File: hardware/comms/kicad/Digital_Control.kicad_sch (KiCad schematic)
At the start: 9 parts, among them J6 Conn_01x20, J7 Conn_01x20, J8 Conn_01x20

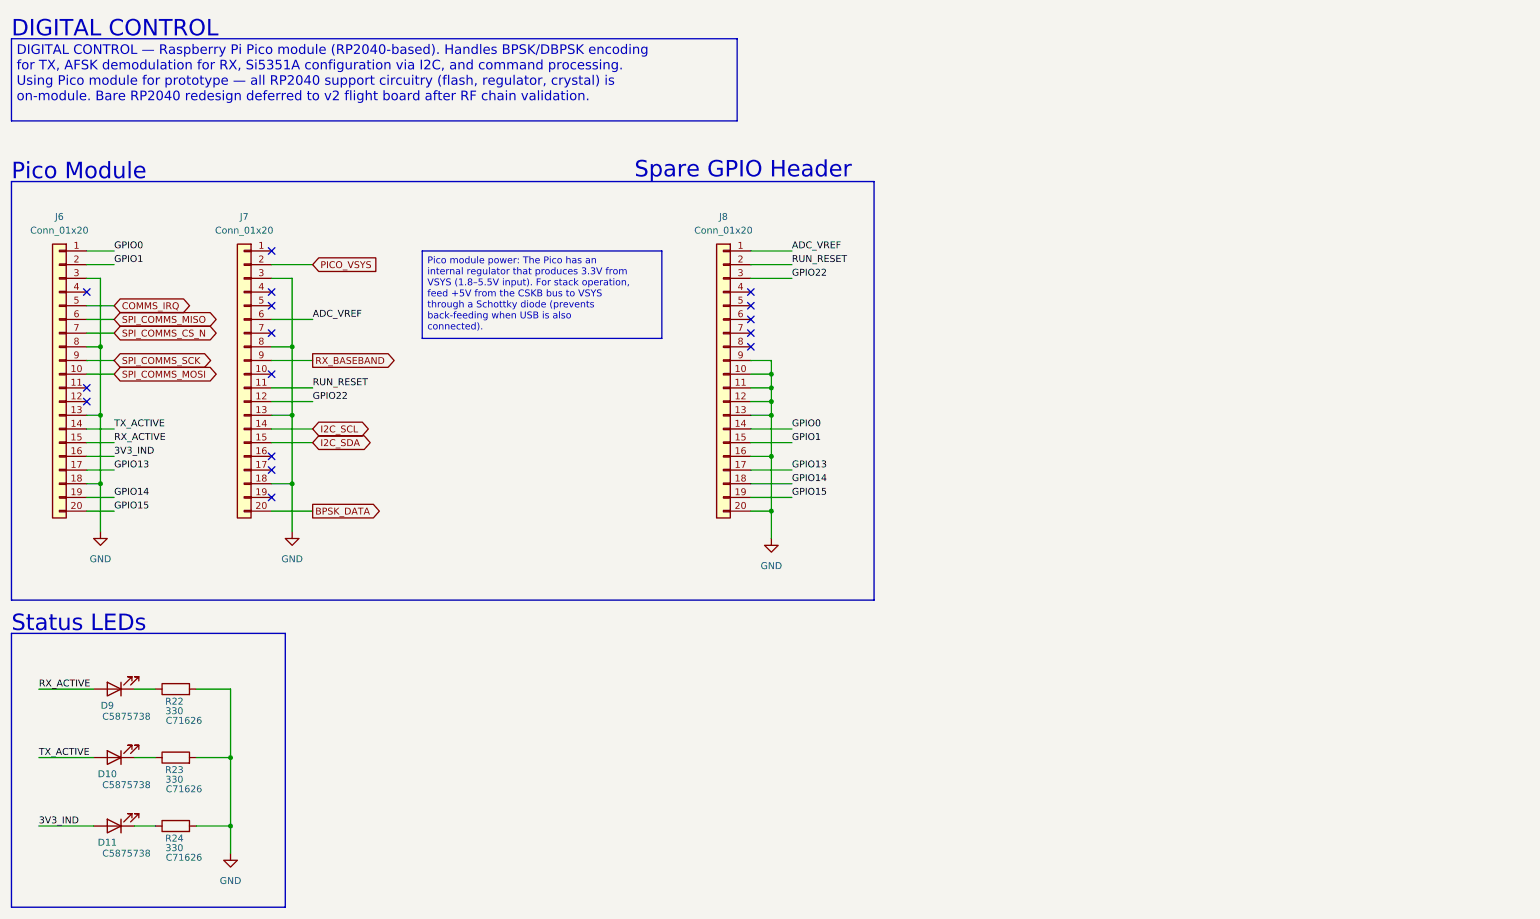
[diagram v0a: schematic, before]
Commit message: comms: checkpoint current KiCad design before ground station work
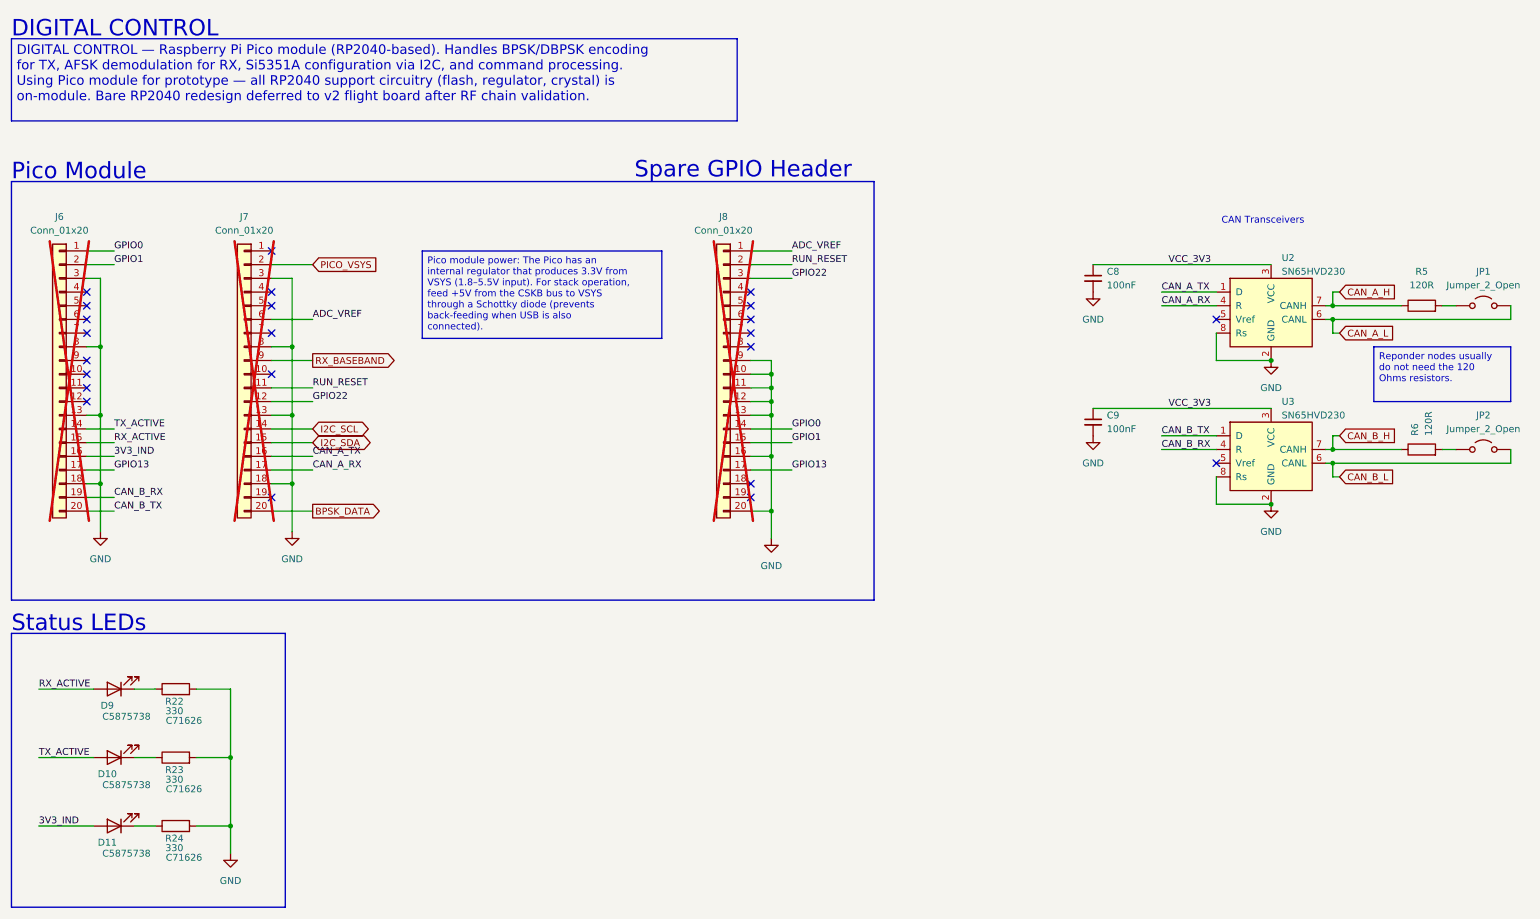
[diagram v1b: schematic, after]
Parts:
- added C8, C9: 100nF, Capacitor_SMD:C_0805_2012Metric, symbol Device:C_Small
- added JP1, JP2: Jumper_2_Open, Connector_PinHeader_2.54mm:PinHeader_1x02_P2.54mm_Vertical, symbol Jumper:Jumper_2_Open
- added R5, R6: 120R, Resistor_SMD:R_0805_2012Metric, symbol Device:R
- added U2, U3: SN65HVD230, Package_SO:SOIC-8_3.9x4.9mm_P1.27mm, symbol Interface_CAN_LIN:SN65HVD230
- J6, J7: footprint (none) -> Connector_PinHeader_2.54mm:PinHeader_1x20_P2.54mm_Vertical; AssemblyNote (none) -> DNP - optional 1x20 2.54mm through-hole header; do not popu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; LCSC Part # ESQ-120-14-G-S -> (none); now not fitted
- J8: footprint (none) -> Connector_PinHeader_2.54mm:PinHeader_1x20_P2.54mm_Vertical; Assembly Note (none) -> DNP - optional 1x20 2.54mm through-hole expansion header; p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; AssemblyNote (none) -> DNP - optional 1x20 2.54mm through-hole header; do not popu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; LCSC Part # ESQ-120-14-G-S -> (none); now not fitted
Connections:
- net GND: now also C8.2, C9.2, U2.2 (GND), U2.8 (Rs), U3.2 (GND), U3.8 (Rs)
- net CAN_A_TX: now reaches J7.16 (Pin_16)
- net CAN_A_TX: now also U2.1 (D)
- net CAN_A_RX: now reaches J7.17 (Pin_17)
- net CAN_A_RX: now also U2.4 (R)
- net COMMS_IRQ: no longer names the net of J6.5 (Pin_5)
- net GPIO14: no longer names the net of J8.18 (Pin_18)
- net GPIO14: no longer J6.19 (Pin_19)
- net GPIO15: no longer names the net of J8.19 (Pin_19)
- net GPIO15: no longer J6.20 (Pin_20)
- net SPI_COMMS_CS_N: no longer names the net of J6.7 (Pin_7)
- net SPI_COMMS_MISO: no longer names the net of J6.6 (Pin_6)
- net SPI_COMMS_MOSI: no longer names the net of J6.10 (Pin_10)
- net SPI_COMMS_SCK: no longer names the net of J6.9 (Pin_9)
- new net: JP1.1 (A), R5.2
- new net: JP2.1 (A), R6.2
- new net CAN_A_H: R5.1, U2.7 (CANH)
- new net CAN_A_L: JP1.2 (B), U2.6 (CANL)
- new net CAN_B_H: R6.1, U3.7 (CANH)
- new net CAN_B_L: JP2.2 (B), U3.6 (CANL)
- new net CAN_B_RX: J6.19 (Pin_19), U3.4 (R)
- new net CAN_B_TX: J6.20 (Pin_20), U3.1 (D)
- new net VCC_3V3: C8.1, C9.1, U2.3 (VCC), U3.3 (VCC)
- no-connect marks 16 -> 23
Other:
- note added: "CAN Transceivers"
